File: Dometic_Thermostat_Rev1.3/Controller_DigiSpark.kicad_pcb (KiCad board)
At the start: 2 copper layers, 82.3 x 63.2 mm, 26 parts, among them P1 UNREG_12V_IN, P2 UNUSED_MICRO_PINS, P3 RELAY_SW_OUT, P4 RELAY_NC, P5 FUSE_BLOCK, P6 AUX_VOLT_CONN, Q1 2N3904, Q2 2N2222A, T1 Relay_SPDT, U1 7805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

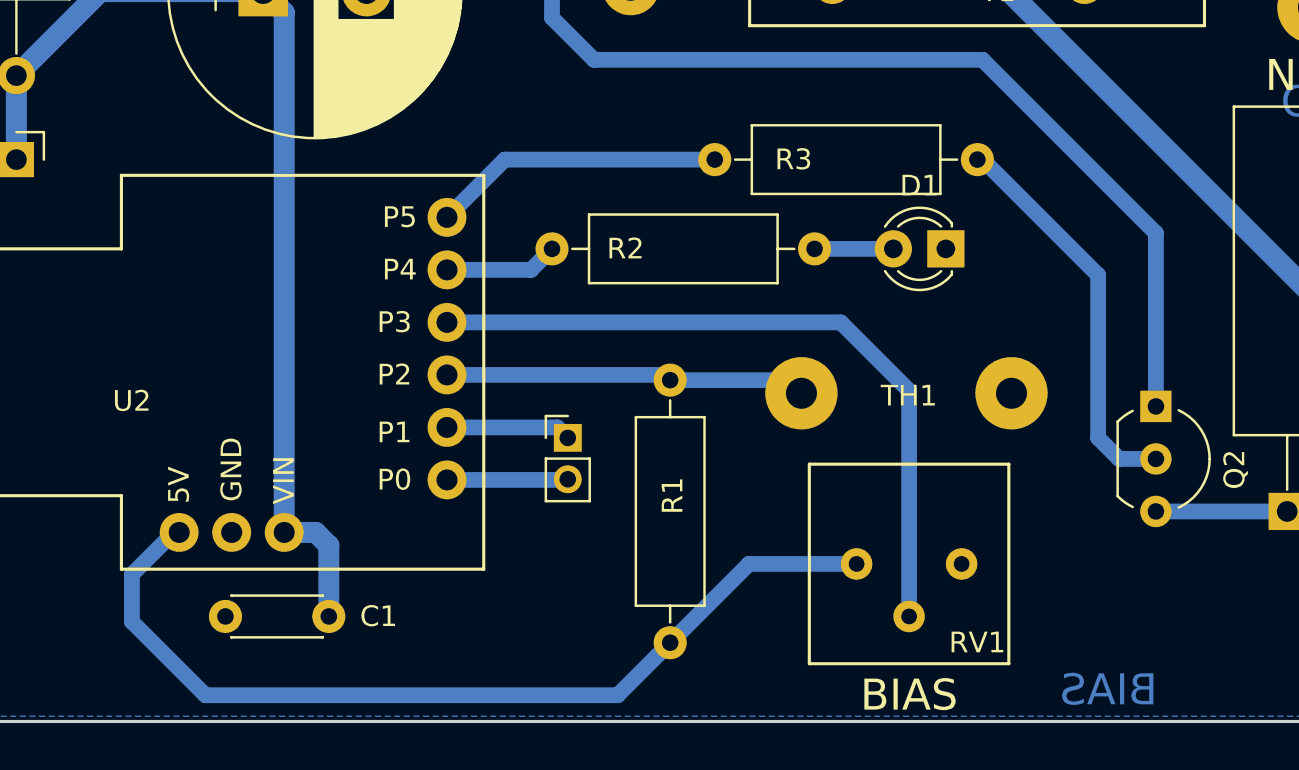
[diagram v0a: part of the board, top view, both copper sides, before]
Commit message: Add R4, change footprints TH1 & LED
Added R4 to board, changed thermistor and LED footprints.
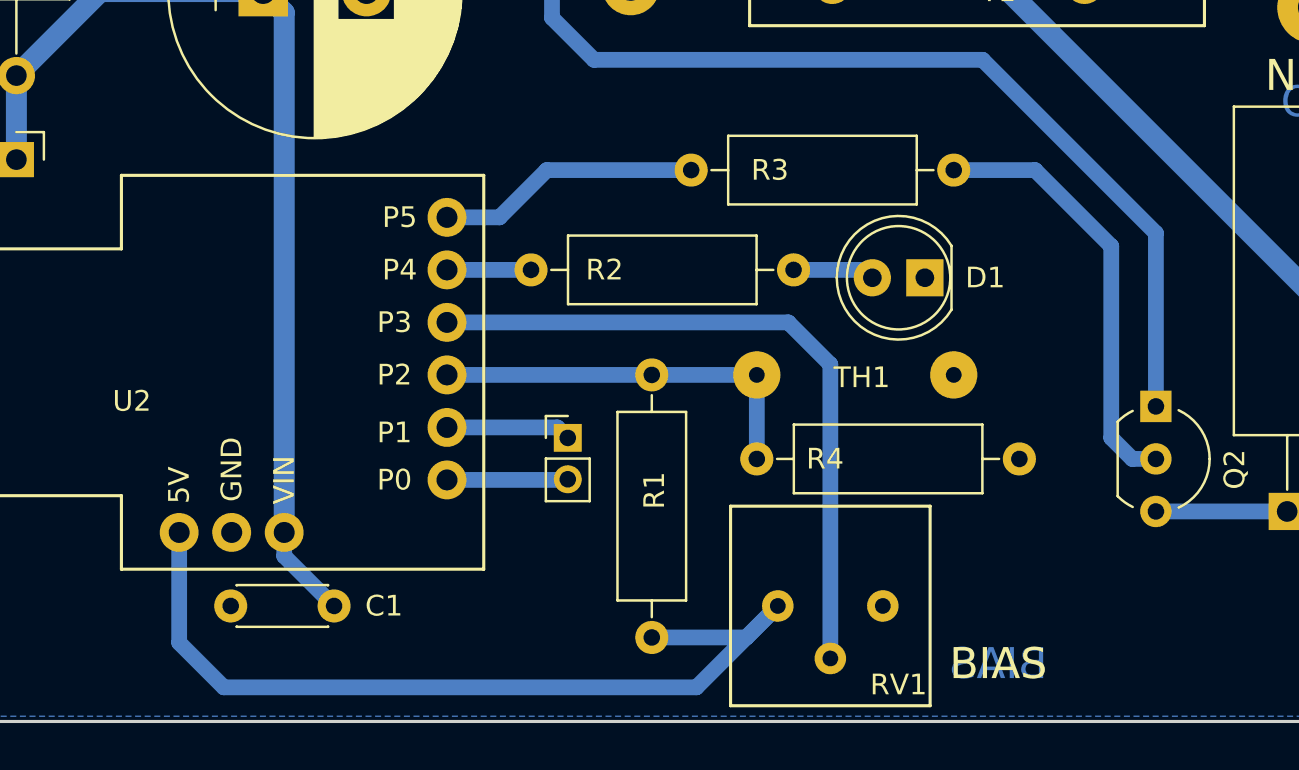
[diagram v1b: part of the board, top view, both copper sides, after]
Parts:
- added R4: R||, Resistors_ThroughHole:R_Axial_DIN0309_L9.0mm_D3.2mm_P12.70mm_Horizontal, F.Cu at (223.5, 153.4)
- D1: footprint LEDs:LED_D3.0mm -> LEDs:LED_D5.0mm
- TH1: footprint COMPLIB:SolderWirePad_2x_1-5mmDrill-CUSTOMWIDE -> COMPLIB:Therm_Wire_Mounts
- moved RV1 4.32 mm to (227.1, 160.5)
- moved TH1 2.93 mm to (228.0, 149.4)
- moved D1 1.73 mm to (231.6, 144.7)
- moved R2 1.44 mm to (225.3, 144.3)
- moved R3 1.25 mm to (233.0, 139.4)
- moved R1 0.92 mm to (218.4, 149.4)
- moved C1 0.57 mm to (203.1, 160.5)
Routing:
- net Net-(R1-Pad1): track 21.3 -> 19.1 mm
- net GND: track 2.12 -> 0.00 mm
- net Net-(Q2-Pad2): track 19.2 -> 21.0 mm
- net Net-(R2-Pad2): track 5.50 -> 4.06 mm
- net Net-(R3-Pad2): track 14.6 -> 13.3 mm
- net Net-(C1-Pad1): track 51.6 -> 50.3 mm
- net Net-(RV1-Pad2): track 34.6 -> 33.6 mm
- net Net-(R1-Pad2): track 44.6 -> 43.8 mm

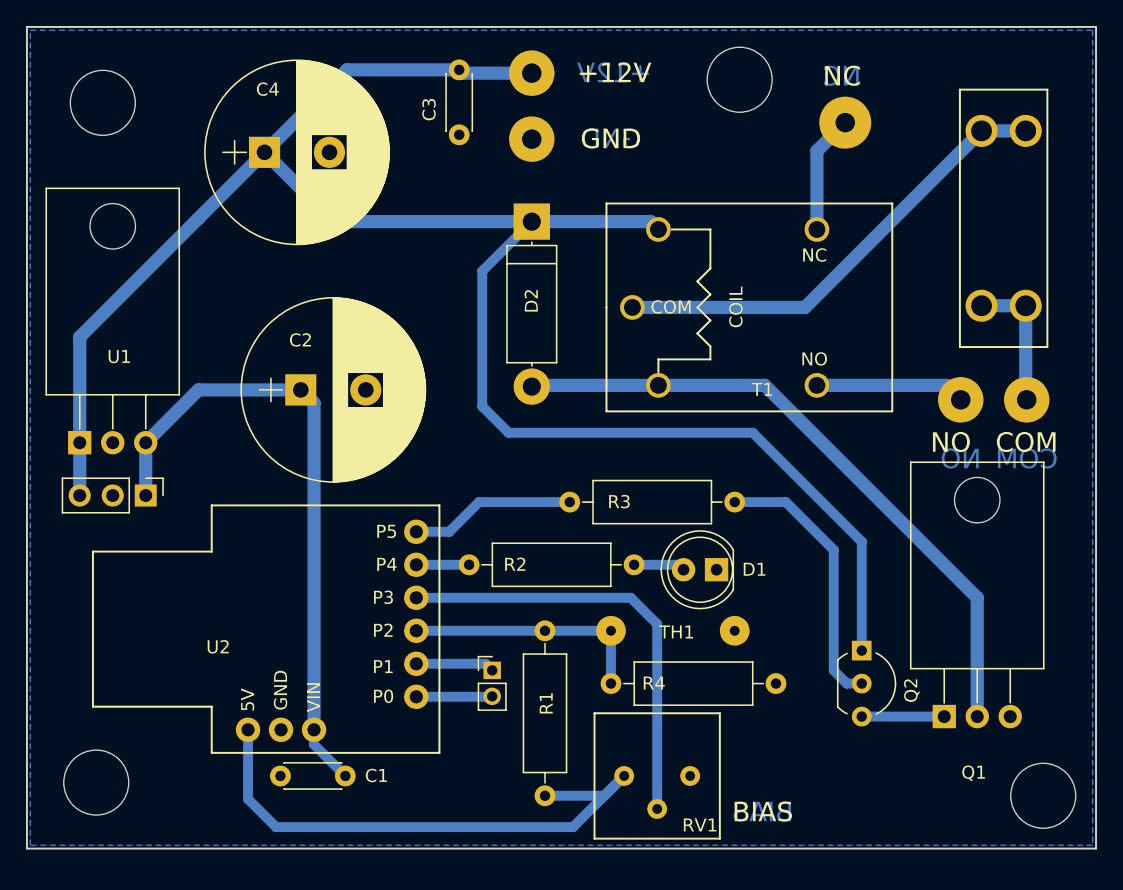
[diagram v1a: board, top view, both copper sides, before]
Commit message: Added test points, provided access to P4
to directly tie LED to relay, cut trace b/w TP2 & TP3.
Jump TP2 to TP1, then TP3 provides access to P4 of micro.
This also cleaned up the ground plane around R2&3
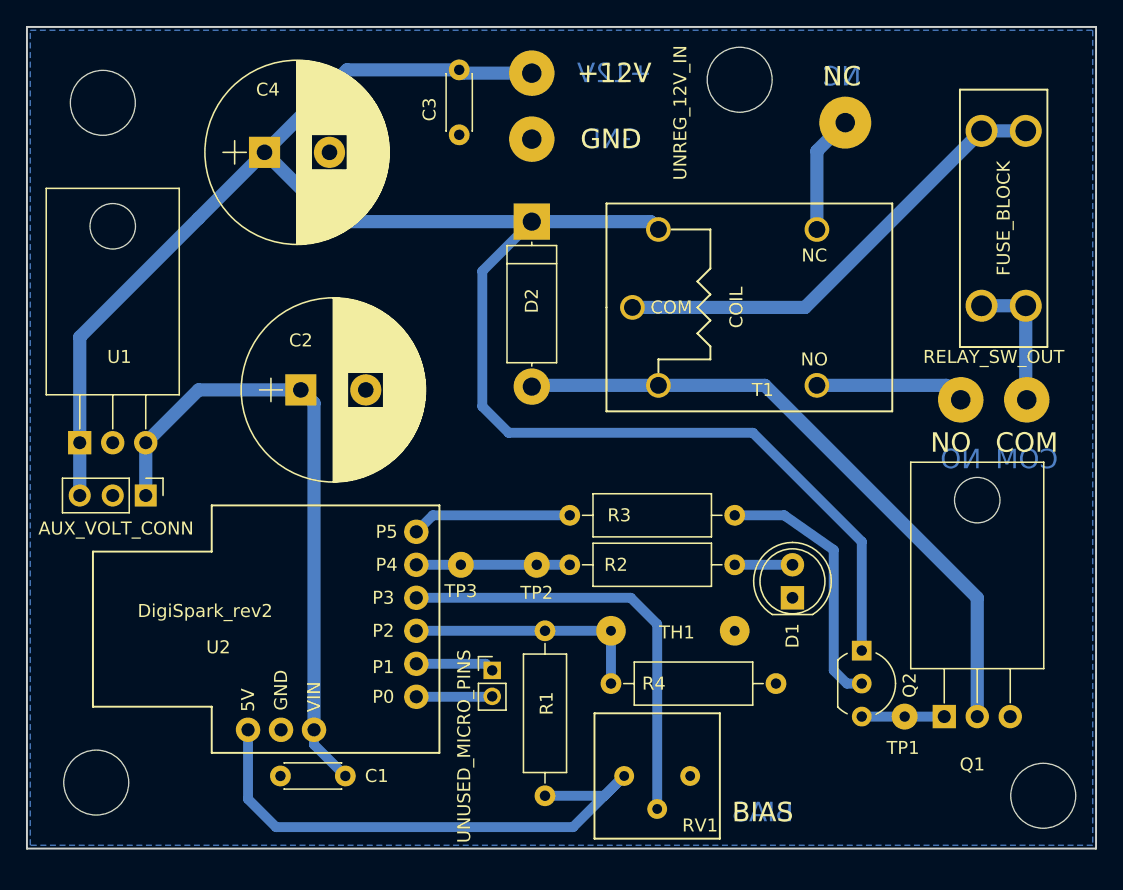
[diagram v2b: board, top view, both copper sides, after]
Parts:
- added TP1: SolderWirePad_single_0-8mmDrill, Wire_Pads:SolderWirePad_single_0-8mmDrill, F.Cu at (246.1, 156.0)
- added TP2: SolderWirePad_single_0-8mmDrill, Wire_Pads:SolderWirePad_single_0-8mmDrill, F.Cu at (217.8, 144.3)
- added TP3: SolderWirePad_single_0-8mmDrill, Wire_Pads:SolderWirePad_single_0-8mmDrill, F.Cu at (212.0, 144.3)
- moved R2 7.75 mm to (233.0, 144.3)
- moved D1 6.23 mm to (237.5, 146.8), turned to 90 degrees
- moved R3 1.02 mm to (233.0, 140.5)
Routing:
- net Net-(R2-Pad2): track 4.06 -> 11.8 mm
- net Net-(Q2-Pad2): track 21.0 -> 20.4 mm
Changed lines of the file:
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@@
     (thickness 1.6)
     (drawings 16)
-    (tracks 78)
+    (tracks 76)
     (zones 0)
-    (modules 27)
+    (modules 30)
     (nets 19)
   )
@@
       (effects (font (size 1 1) (thickness 0.15)))
     )
-    (fp_text value UNUSED_MICRO_PINS (at -2.159 5.842 90) (layer F.Fab)
+    (fp_text value UNUSED_MICRO_PINS (at -2.159 5.842 90) (layer F.SilkS)
       (effects (font (size 1 1) (thickness 0.15)))
     )
@@
       (effects (font (size 1 1) (thickness 0.15)))
     )
-    (fp_text value UNREG_12V_IN (at -0.508 11.43 90) (layer F.Fab)
+    (fp_text value UNREG_12V_IN (at -0.508 11.43 90) (layer F.SilkS)
       (effects (font (size 1 1) (thickness 0.15)))
     )
@@
       (effects (font (size 1 1) (thickness 0.15)))
     )
-    (fp_text value RELAY_SW_OUT (at 0 -3.302) (layer F.Fab)
+    (fp_text value RELAY_SW_OUT (at 0 -3.302) (layer F.SilkS)
       (effects (font (size 1 1) (thickness 0.15)))
     )
@@
       (effects (font (size 1 1) (thickness 0.15)))
     )
-    (fp_text value FUSE_BLOCK (at 0 0 90) (layer F.Fab)
+    (fp_text value FUSE_BLOCK (at 0 0 90) (layer F.SilkS)
       (effects (font (size 1 1) (thickness 0.15)))
     )
@@
     (descr "TO-220, Horizontal, RM 2.54mm")
     (tags "TO-220 Horizontal RM 2.54mm")
-    (fp_text reference Q1 (at 2.286 4.318) (layer F.SilkS)
+    (fp_text reference Q1 (at 2.159 3.683) (layer F.SilkS)
       (effects (font (size 1 1) (thickness 0.15)))
     )
@@
   )
   (module Resistors_ThroughHole:R_Axial_DIN0309_L9.0mm_D3.2mm_P12.70mm_Horizontal (layer F.Cu)
-    (at 225.298 144.272 180)
+    (at 233.045 144.272 180)
     (descr "Resistor, Axial_DIN0309 series, Axial, Horizontal, pin pitch=12.7mm, 0.5W = 1/2W, length*diameter=9*3.2mm^2, http://cdn-reichelt.de/documents/datenblatt/B400/1_4W%23YAG.pdf")
     (tags "Resistor Axial_DIN0309 series Axial Horizontal pin pitch 12.7mm 0.5W = 1/2W length 9mm diameter 3.2mm")
@@
   )
   (module Resistors_ThroughHole:R_Axial_DIN0309_L9.0mm_D3.2mm_P12.70mm_Horizontal (layer F.Cu)
-    (at 233.045 139.446 180)
+    (at 233.045 140.462 180)
     (descr "Resistor, Axial_DIN0309 series, Axial, Horizontal, pin pitch=12.7mm, 0.5W = 1/2W, length*diameter=9*3.2mm^2, http://cdn-reichelt.de/documents/datenblatt/B400/1_4W%23YAG.pdf")
     (tags "Resistor Axial_DIN0309 series Axial Horizontal pin pitch 12.7mm 0.5W = 1/2W length 9mm diameter 3.2mm")
@@
       (effects (font (size 1 1) (thickness 0.15)))
     )
-    (fp_text value DigiSpark_rev2 (at 143.764 103.632) (layer F.Fab)
+    (fp_text value DigiSpark_rev2 (at 143.764 103.632) (layer F.SilkS)
       (effects (font (size 1 1) (thickness 0.15)))
     )
@@
       (effects (font (size 1 1) (thickness 0.15)))
     )
-    (fp_text value AUX_VOLT_CONN (at 2.54 2.286 360) (layer F.Fab)
+    (fp_text value AUX_VOLT_CONN (at 2.54 2.286 360) (layer F.SilkS)
       (effects (font (size 1 1) (thickness 0.15)))
     )
@@
     (descr "TO-92 leads in-line, wide, drill 0.8mm (see NXP sot054_po.pdf)")
     (tags "to-92 sc-43 sc-43a sot54 PA33 transistor")
-    (fp_text reference Q2 (at 3.048 -3.81 450) (layer F.SilkS)
+    (fp_text reference Q2 (at 2.667 -3.683 450) (layer F.SilkS)
       (effects (font (size 1 1) (thickness 0.15)))
     )
@@
   )
   (module LEDs:LED_D5.0mm (layer F.Cu)
-    (at 231.648 144.653 180)
+    (at 237.49 146.812 90)
     (descr "LED, diameter 5.0mm, 2 pins, http://cdn-reichelt.de/documents/datenblatt/A500/LL-504BC2E-009.pdf")
     (tags "LED diameter 5.0mm 2 pins")
-    (fp_text reference D1 (at -2.921 0 180) (layer F.SilkS)
-      (effects (font (size 1 1) (thickness 0.15)))
-    )
-    (fp_text value LED (at -2.921 -1.524 180) (layer F.Fab)
+    (fp_text reference D1 (at -2.921 0 90) (layer F.SilkS)
+      (effects (font (size 1 1) (thickness 0.15)))
+    )
+    (fp_text value LED (at -2.921 -1.524 90) (layer F.Fab)
       (effects (font (size 1 1) (thickness 0.15)))
     )
@@
     (fp_line (start 4.5 3.25) (end 4.5 -3.25) (layer F.CrtYd) (width 0.05))
     (fp_line (start 4.5 -3.25) (end -1.95 -3.25) (layer F.CrtYd) (width 0.05))
-    (pad 1 thru_hole rect (at 0 0 180) (size 1.8 1.8) (drill 0.9) (layers *.Cu *.Mask)
+    (pad 1 thru_hole rect (at 0 0 90) (size 1.8 1.8) (drill 0.9) (layers *.Cu *.Mask)
       (net 2 GND))
-    (pad 2 thru_hole circle (at 2.54 0 180) (size 1.8 1.8) (drill 0.9) (layers *.Cu *.Mask)
+    (pad 2 thru_hole circle (at 2.54 0 90) (size 1.8 1.8) (drill 0.9) (layers *.Cu *.Mask)
       (net 4 "Net-(D1-Pad2)"))
     (model LEDs.3dshapes/LED_D5.0mm.wrl
@@
       (rotate (xyz 0 0 0))
     )
+  )
+  (module Wire_Pads:SolderWirePad_single_0-8mmDrill (layer F.Cu)
+    (at 246.126 155.956)
+    (fp_text reference TP1 (at -0.127 2.413) (layer F.SilkS)
+      (effects (font (size 1 1) (thickness 0.15)))
+    )
+    (fp_text value SolderWirePad_single_0-8mmDrill (at -0.381 13.081) (layer F.Fab)
+      (effects (font (size 1 1) (thickness 0.15)))
+    )
+    (pad 1 thru_hole circle (at 0 0) (size 1.99898 1.99898) (drill 0.8001) (layers *.Cu *.Mask))
+  )
+  (module Wire_Pads:SolderWirePad_single_0-8mmDrill (layer F.Cu)
+    (at 211.963 144.272)
+    (fp_text reference TP3 (at 0 2.032) (layer F.SilkS)
+      (effects (font (size 1 1) (thickness 0.15)))
+    )
+    (fp_text value SolderWirePad_single_0-8mmDrill (at 3.81 25.4) (layer F.Fab)
+      (effects (font (size 1 1) (thickness 0.15)))
+    )
+    (pad 1 thru_hole circle (at 0 0) (size 1.99898 1.99898) (drill 0.8001) (layers *.Cu *.Mask))
+  )
+  (module Wire_Pads:SolderWirePad_single_0-8mmDrill (layer F.Cu)
+    (at 217.805 144.272)
+    (fp_text reference TP2 (at 0 2.159) (layer F.SilkS)
+      (effects (font (size 1 1) (thickness 0.15)))
+    )
+    (fp_text value SolderWirePad_single_0-8mmDrill (at -29.591 24.765) (layer F.Fab)
+      (effects (font (size 1 1) (thickness 0.15)))
+    )
+    (pad 1 thru_hole circle (at 0 0) (size 1.99898 1.99898) (drill 0.8001) (layers *.Cu *.Mask))
   )
   (gr_text BIAS (at 235.204 163.322) (layer F.SilkS)
@@
   (segment (start 226.568 117.856) (end 227.172 118.46) (width 1.016) (layer B.Cu) (net 3))
   (segment (start 218.028 118.46) (end 217.424 117.856) (width 0.25) (layer B.Cu) (net 3))
-  (segment (start 225.298 144.272) (end 228.727 144.272) (width 0.762) (layer B.Cu) (net 4))
-  (segment (start 228.727 144.272) (end 229.108 144.653) (width 0.762) (layer B.Cu) (net 4))
+  (segment (start 233.045 144.272) (end 237.49 144.272) (width 0.762) (layer B.Cu) (net 4))
   (segment (start 227.172 130.46) (end 235.362 130.46) (width 1.016) (layer B.Cu) (net 5))
   (segment (start 251.714 146.812) (end 251.714 155.956) (width 1.016) (layer B.Cu) (net 5))
@@
   (segment (start 195.58 162.306) (end 197.739 164.465) (width 0.762) (layer B.Cu) (net 14))
   (segment (start 195.58 156.972) (end 195.326 156.972) (width 0.762) (layer B.Cu) (net 14))
-  (segment (start 208.534 144.272) (end 212.598 144.272) (width 0.762) (layer B.Cu) (net 15))
-  (segment (start 208.534 141.732) (end 211.074 141.732) (width 0.762) (layer B.Cu) (net 16))
-  (segment (start 213.36 139.446) (end 220.345 139.446) (width 0.762) (layer B.Cu) (net 16))
-  (segment (start 211.074 141.732) (end 213.36 139.446) (width 0.762) (layer B.Cu) (net 16))
+  (segment (start 208.534 144.272) (end 220.345 144.272) (width 0.762) (layer B.Cu) (net 15))
+  (segment (start 220.345 140.462) (end 209.804 140.462) (width 0.762) (layer B.Cu) (net 16) (status 400000))
+  (segment (start 209.804 140.462) (end 208.534 141.732) (width 0.762) (layer B.Cu) (net 16) (status 800000))
   (segment (start 208.534 141.732) (end 209.042 141.732) (width 0.508) (layer B.Cu) (net 16))
   (segment (start 208.534 146.812) (end 225.044 146.812) (width 0.762) (layer B.Cu) (net 17))
@@
   (segment (start 225.044 146.812) (end 227.076 148.844) (width 0.762) (layer B.Cu) (net 17))
   (segment (start 242.824 153.416) (end 241.681 153.416) (width 0.762) (layer B.Cu) (net 18))
-  (segment (start 236.982 139.446) (end 233.045 139.446) (width 0.762) (layer B.Cu) (net 18))
-  (segment (start 240.665 143.129) (end 236.982 139.446) (width 0.762) (layer B.Cu) (net 18))
+  (segment (start 236.855 140.462) (end 232.918 140.462) (width 0.762) (layer B.Cu) (net 18))
+  (segment (start 240.665 143.129) (end 236.855 140.462) (width 0.762) (layer B.Cu) (net 18))
   (segment (start 240.665 152.4) (end 240.665 143.129) (width 0.762) (layer B.Cu) (net 18))
   (segment (start 241.681 153.416) (end 240.665 152.4) (width 0.762) (layer B.Cu) (net 18))

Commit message: Added logo to B Cu
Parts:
- added ?: LOGO, COMPLIB:LOGO_0-5IN_FCu, B.Cu at (185.5, 153.5)
- REF**: moved to B.Cu
